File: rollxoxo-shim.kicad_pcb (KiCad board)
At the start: 4 copper layers, 29 x 42 mm, 68 parts, among them J1 USB_C_Receptacle_USB2.0_14P, J2 Conn_01x02, J3 Conn_01x10, J4 Conn_01x01, J5 Conn_01x10, J6 Conn_01x03, J7 Conn_01x01, SW1 SW_Push, SW2 SW_Push, U1 SN74LV1T125DBV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

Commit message: pcb: reorganize programmable gpios
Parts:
- moved R9 19.0 mm to (80.7, 153.8)
- moved R8 17.0 mm to (80.8, 154.8), turned to 0 degrees
- moved C19 0.25 mm to (80.8, 152.0)
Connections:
- U6 pad 14: /FLASH -> unconnected-(U6-GPIO9/ADC1_CH8-Pad14)
- U6 pad 6: unconnected-(U6-GPIO1/ADC1_CH0-Pad6) -> /FLASH
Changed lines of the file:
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@@
 	(footprint "Capacitor_SMD:C_0402_1005Metric"
 		(layer "F.Cu")
-		(at 80.75 152.25)
+		(at 80.75 152)
 		(descr "Capacitor SMD 0402 (1005 Metric), square (rectangular) end terminal, IPC-7351 nominal, (Body size source: IPC-SM-782 page 76, https://www.pcb-3d.com/wordpress/wp-content/uploads/ipc-sm-782a_amendment_1_and_2.pdf)")
 		(tags "capacitor")
@@
 			(layers "F.Cu" "F.Mask" "F.Paste")
 			(roundrect_rratio 0.25)
-			(net "unconnected-(U6-GPIO1{slash}ADC1_CH0-Pad6)")
+			(net "/FLASH")
 			(pinfunction "GPIO1/ADC1_CH0_6")
-			(pintype "bidirectional+no_connect")
+			(pintype "bidirectional")
 		)
 		(pad "7" smd roundrect
@@
 			(layers "F.Cu" "F.Mask" "F.Paste")
 			(roundrect_rratio 0.25)
-			(net "/FLASH")
+			(net "unconnected-(U6-GPIO9{slash}ADC1_CH8-Pad14)")
 			(pinfunction "GPIO9/ADC1_CH8_14")
-			(pintype "bidirectional")
+			(pintype "bidirectional+no_connect")
 		)
 		(pad "15" smd roundrect
@@
 	(footprint "Resistor_SMD:R_0402_1005Metric"
 		(layer "F.Cu")
-		(at 61.75 154.5)
+		(at 80.74 153.75)
 		(descr "Resistor SMD 0402 (1005 Metric), square (rectangular) end terminal, IPC-7351 nominal, (Body size source: IPC-SM-782 page 72, https://www.pcb-3d.com/wordpress/wp-content/uploads/ipc-sm-782a_amendment_1_and_2.pdf)")
 		(tags "resistor")
@@
 	(footprint "Resistor_SMD:R_0402_1005Metric"
 		(layer "F.Cu")
-		(at 63.76 154.5 180)
+		(at 80.76 154.75)
 		(descr "Resistor SMD 0402 (1005 Metric), square (rectangular) end terminal, IPC-7351 nominal, (Body size source: IPC-SM-782 page 72, https://www.pcb-3d.com/wordpress/wp-content/uploads/ipc-sm-782a_amendment_1_and_2.pdf)")
 		(tags "resistor")
@@
 		)
 		(property "Basic" "Y"
-			(at 0 0 180)
+			(at 0 0 0)
 			(unlocked yes)
 			(layer "F.Fab")
@@
 		)
 		(property "JLCPCB Part #" "C25744"
-			(at 0 0 180)
+			(at 0 0 0)
 			(unlocked yes)
 			(layer "F.Fab")
@@
 		)
 		(property "Manufacturer" "Uniroyal Elec"
-			(at 0 0 180)
+			(at 0 0 0)
 			(unlocked yes)
 			(layer "F.Fab")
@@
 		)
 		(property "Manufacturer Part Number" "0402WGF1002TCE"
-			(at 0 0 180)
+			(at 0 0 0)
 			(unlocked yes)
 			(layer "F.Fab")
@@
 		(duplicate_pad_numbers_are_jumpers no)
 		(fp_line
-			(start -0.153641 0.38)
-			(end 0.153641 0.38)
+			(start -0.153641 -0.38)
+			(end 0.153641 -0.38)
 			(stroke
 				(width 0.12)
@@
 		)
 		(fp_line
-			(start -0.153641 -0.38)
-			(end 0.153641 -0.38)
+			(start -0.153641 0.38)
+			(end 0.153641 0.38)
 			(stroke
 				(width 0.12)
@@
 		)
 		(pad "1" smd roundrect
-			(at -0.51 0 180)
+			(at -0.51 0)
 			(size 0.54 0.64)
 			(layers "F.Cu" "F.Mask" "F.Paste")
@@
 		)
 		(pad "2" smd roundrect
-			(at 0.51 0 180)
+			(at 0.51 0)
 			(size 0.54 0.64)
 			(layers "F.Cu" "F.Mask" "F.Paste")
@@
 	)
 	(via
-		(at 81.25 153)
+		(at 81.25 152.75)
 		(size 0.7)
 		(drill 0.3)

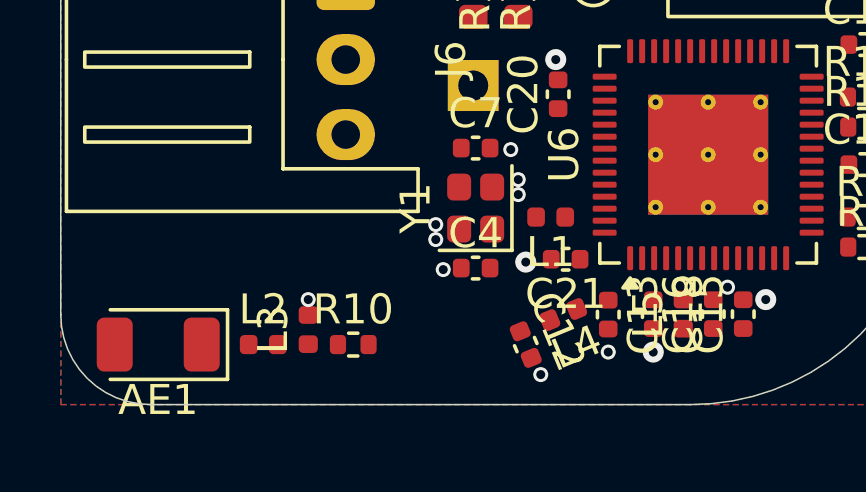
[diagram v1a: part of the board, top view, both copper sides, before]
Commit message: pcb: add rf routing
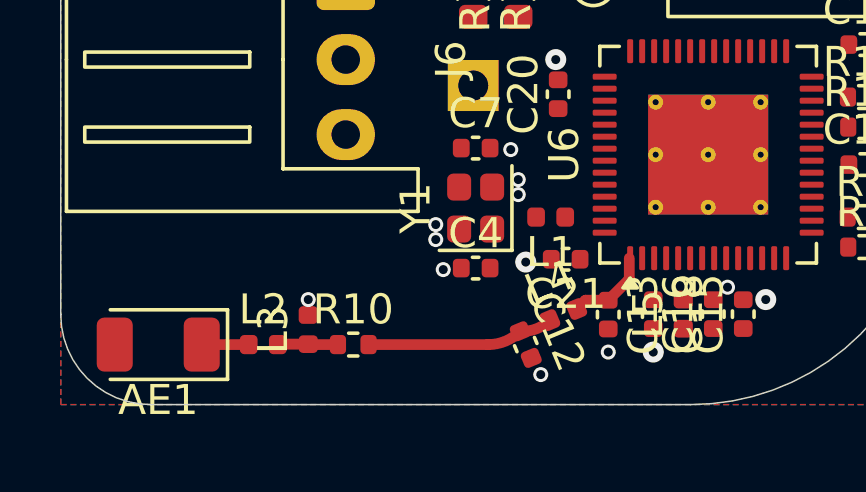
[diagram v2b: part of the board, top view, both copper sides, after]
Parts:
- turned L4 to 22.5 degrees
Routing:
- net /RF_TRANS: track 0.00 -> 6.25 mm
- net /RF_ESP: track 0.00 -> 2.86 mm
- net Net-(L2-Pad2): track 0.00 -> 2.02 mm
- net /RF_ANT: track 0.00 -> 1.56 mm
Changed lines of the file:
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@@
 	(footprint "Inductor_SMD:L_0402_1005Metric"
 		(layer "F.Cu")
-		(at 70.75 157 -157.5)
+		(at 70.75 157 22.5)
 		(descr "Inductor SMD 0402 (1005 Metric), square (rectangular) end terminal, IPC-7351 nominal, (Body size source: http://www.tortai-tech.com/upload/download/2011102023233369053.pdf)")
 		(tags "inductor")
@@
 		)
 		(property "Manufacturer" "Murata"
-			(at 0 0 202.5)
+			(at 0 0 22.5)
 			(unlocked yes)
 			(layer "F.Fab")
@@
 		)
 		(property "Manufacturer Part Number" "LQG15HS2N7S02D"
-			(at 0 0 202.5)
+			(at 0 0 22.5)
 			(unlocked yes)
 			(layer "F.Fab")
@@
 		)
 		(property "Basic" "X"
-			(at 0 0 202.5)
+			(at 0 0 22.5)
 			(unlocked yes)
 			(layer "F.Fab")
@@
 		)
 		(property "JLCPCB Part #" "C77108"
-			(at 0 0 202.5)
+			(at 0 0 22.5)
 			(unlocked yes)
 			(layer "F.Fab")
@@
 		)
 		(pad "1" smd roundrect
-			(at -0.485 0.000001 202.5)
+			(at -0.485 0.000001 22.5)
 			(size 0.59 0.64)
 			(layers "F.Cu" "F.Mask" "F.Paste")
@@
 		)
 		(pad "2" smd roundrect
-			(at 0.485 -0.000001 202.5)
+			(at 0.485 -0.000001 22.5)
 			(size 0.59 0.64)
 			(layers "F.Cu" "F.Mask" "F.Paste")
@@
 		(net "GND")
 	)
+	(segment
+		(start 60.265 158)
+		(end 58.7 158)
+		(width 0.359)
+		(layer "F.Cu")
+		(net "/RF_ANT")
+	)
+	(segment
+		(start 63.24 158)
+		(end 62.265 158)
+		(width 0.359)
+		(layer "F.Cu")
+		(net "Net-(L2-Pad2)")
+	)
+	(segment
+		(start 62.265 158)
+		(end 62.25 157.985)
+		(width 0.359)
+		(layer "F.Cu")
+		(net "Net-(L2-Pad2)")
+	)
+	(segment
+		(start 61.25 157.985)
+		(end 61.235 158)
+		(width 0.359)
+		(layer "F.Cu")
+		(net "Net-(L2-Pad2)")
+	)
+	(segment
+		(start 62.25 157.985)
+		(end 61.25 157.985)
+		(width 0.359)
+		(layer "F.Cu")
+		(net "Net-(L2-Pad2)")
+	)
+	(segment
+		(start 71.492479 156.52)
+		(end 71.198081 156.814398)
+		(width 0.359)
+		(layer "F.Cu")
+		(net "/RF_ESP")
+	)
+	(segment
+		(start 72.9505 155.8195)
+		(end 72.9505 155.12)
+		(width 0.359)
+		(layer "F.Cu")
+		(net "/RF_ESP")
+	)
+	(segment
+		(start 72.25 156.52)
+		(end 72.9505 155.8195)
+		(width 0.359)
+		(layer "F.Cu")
+		(net "/RF_ESP")
+	)
+	(segment
+		(start 72.25 156.52)
+		(end 71.492479 156.52)
+		(width 0.359)
+		(layer "F.Cu")
+		(net "/RF_ESP")
+	)
+	(segment
+		(start 69.4064 157.556538)
+		(end 69.316312 157.556538)
+		(width 0.359)
+		(layer "F.Cu")
+		(net "/RF_TRANS")
+	)
+	(segment
+		(start 68.2457 158)
+		(end 64.26 158)
+		(width 0.359)
+		(layer "F.Cu")
+		(net "/RF_TRANS")
+	)
+	(arc
+		(start 70.301919 157.185602)
+		(mid 69.891051 157.460135)
+		(end 69.4064 157.556538)
+		(width 0.359)
+		(layer "F.Cu")
+		(net "/RF_TRANS")
+	)
+	(arc
+		(start 69.316312 157.556538)
+		(mid 68.825111 157.884748)
+		(end 68.2457 158)
+		(width 0.359)
+		(layer "F.Cu")
+		(net "/RF_TRANS")
+	)
 	(zone

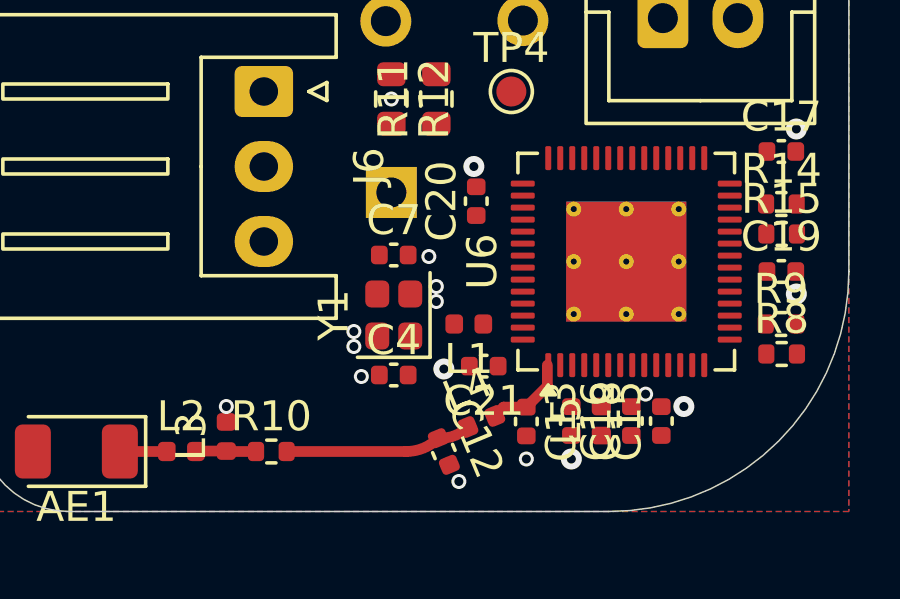
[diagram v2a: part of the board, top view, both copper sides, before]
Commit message: pcb: add rf routing
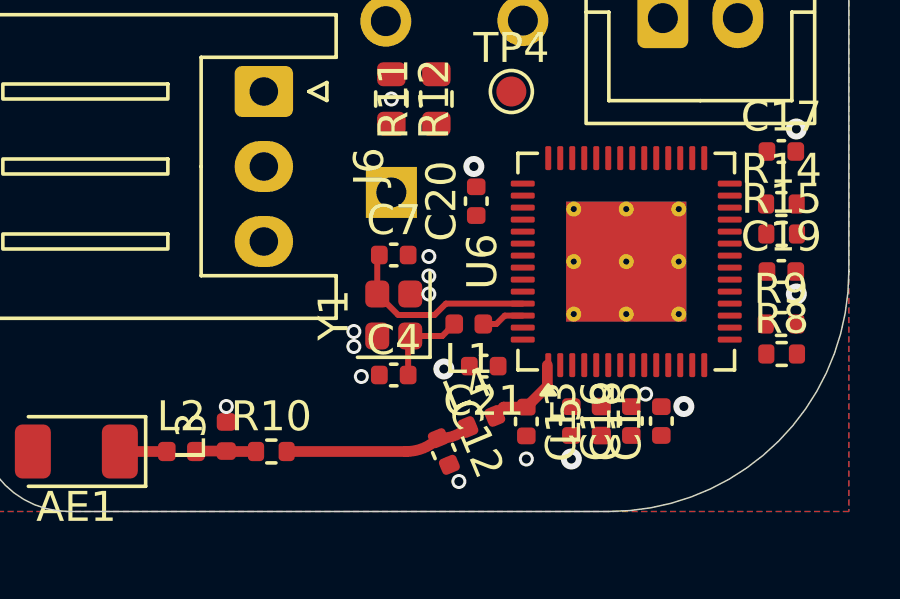
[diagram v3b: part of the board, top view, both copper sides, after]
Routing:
- net /XTAL_N: track 0.00 -> 6.63 mm
- net /XTAL_PL: track 0.00 -> 2.96 mm
- net /XTAL_P: track 0.00 -> 1.43 mm
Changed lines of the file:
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@@
-	)
-	(via
-		(at 69.25 153)
-		(size 0.5)
-		(drill 0.3)
-		(layers "F.Cu" "B.Cu")
-		(free yes)
-		(net "GND")
 	)
 	(via
@@
 	)
 	(via
+		(at 69 152.75)
+		(size 0.5)
+		(drill 0.3)
+		(layers "F.Cu" "B.Cu")
+		(free yes)
+		(net "GND")
+	)
+	(via
 		(at 75 141.25)
 		(size 0.9)
@@
 	)
 	(via
-		(at 69.25 152.5)
+		(at 69 152.150003)
 		(size 0.5)
 		(drill 0.3)
@@
 		(free yes)
 		(net "GND")
+	)
+	(segment
+		(start 67.28 151.52)
+		(end 67.35 151.45)
+		(width 0.2)
+		(layer "F.Cu")
+		(net "/XTAL_N")
+	)
+	(segment
+		(start 69.19 153.45)
+		(end 67.98 153.45)
+		(width 0.2)
+		(layer "F.Cu")
+		(net "/XTAL_N")
+	)
+	(segment
+		(start 69.57 153.07)
+		(end 69.19 153.45)
+		(width 0.2)
+		(layer "F.Cu")
+		(net "/XTAL_N")
+	)
+	(segment
+		(start 72.13 153.07)
+		(end 69.57 153.07)
+		(width 0.2)
+		(layer "F.Cu")
+		(net "/XTAL_N")
+	)
+	(segment
+		(start 67.98 153.45)
+		(end 67.28 152.75)
+		(width 0.2)
+		(layer "F.Cu")
+		(net "/XTAL_N")
+	)
+	(segment
+		(start 67.28 152.75)
+		(end 67.28 151.52)
+		(width 0.2)
+		(layer "F.Cu")
+		(net "/XTAL_N")
 	)
 	(segment
@@
 	)
 	(segment
+		(start 71.25 153.75)
+		(end 71.53 153.47)
+		(width 0.2)
+		(layer "F.Cu")
+		(net "/XTAL_P")
+	)
+	(segment
+		(start 70.815 153.75)
+		(end 71.25 153.75)
+		(width 0.2)
+		(layer "F.Cu")
+		(net "/XTAL_P")
+	)
+	(segment
+		(start 71.53 153.47)
+		(end 72.13 153.47)
+		(width 0.2)
+		(layer "F.Cu")
+		(net "/XTAL_P")
+	)
+	(segment
+		(start 69.845 153.75)
+		(end 69.445 154.15)
+		(width 0.2)
+		(layer "F.Cu")
+		(net "/XTAL_PL")
+	)
+	(segment
+		(start 69.445 154.15)
+		(end 68.38 154.15)
+		(width 0.2)
+		(layer "F.Cu")
+		(net "/XTAL_PL")
+	)
+	(segment
+		(start 68.31 154.22)
+		(end 68.38 154.15)
+		(width 0.2)
+		(layer "F.Cu")
+		(net "/XTAL_PL")
+	)
+	(segment
+		(start 68.31 155.45)
+		(end 68.31 154.22)
+		(width 0.2)
+		(layer "F.Cu")
+		(net "/XTAL_PL")
+	)
+	(segment

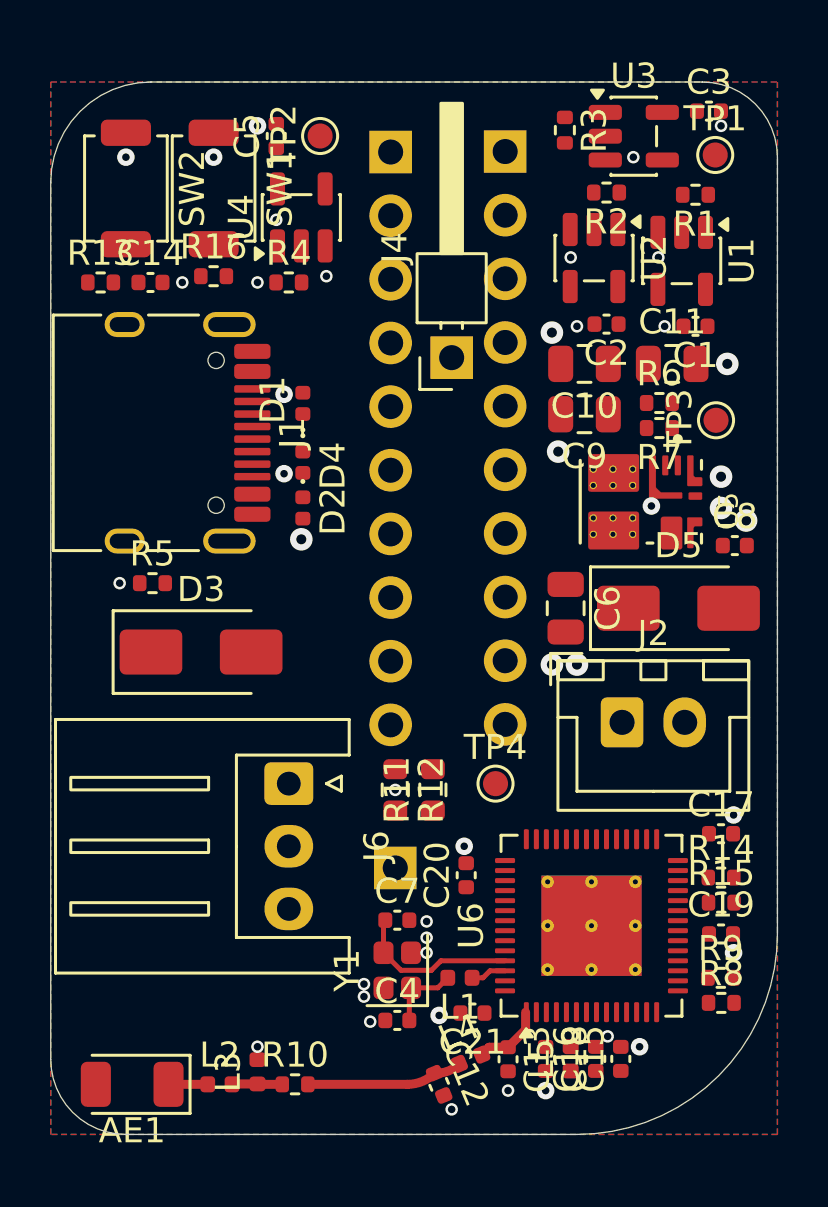
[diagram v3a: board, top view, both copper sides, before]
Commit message: pcb: add usb routing
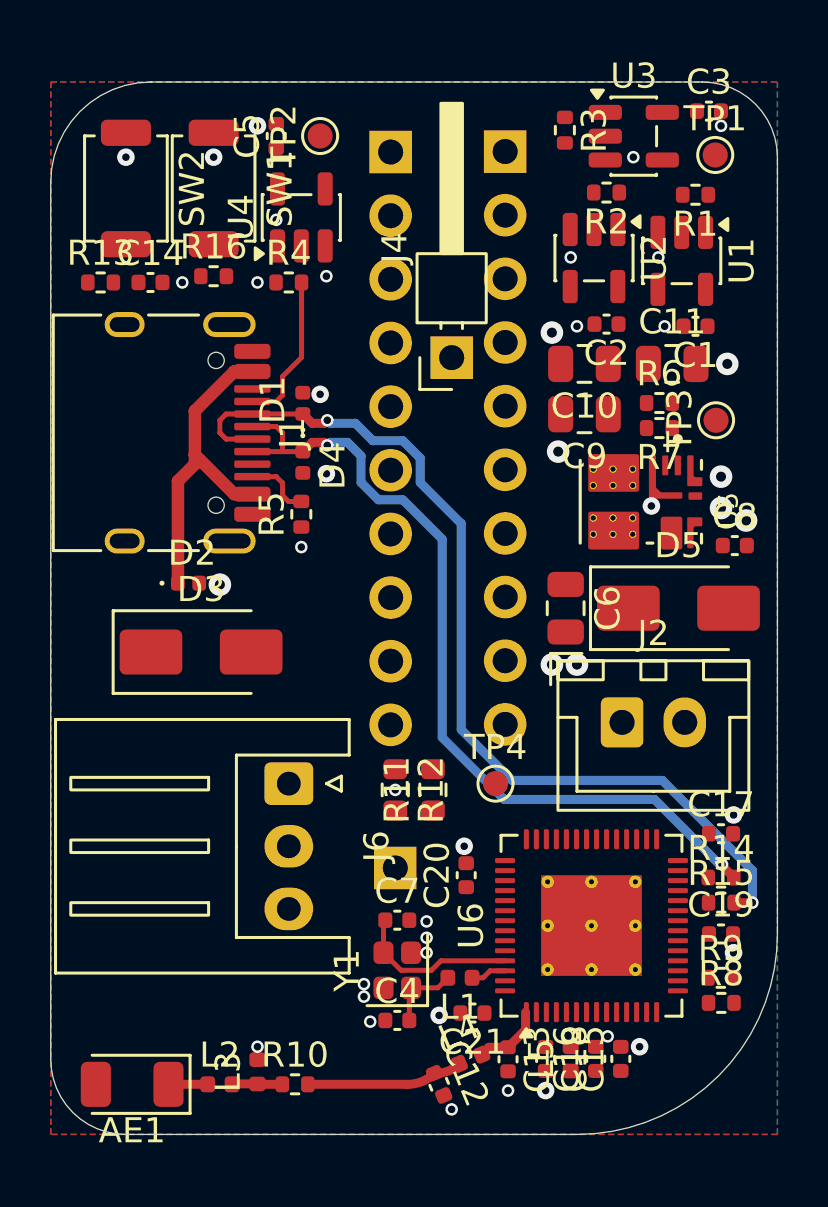
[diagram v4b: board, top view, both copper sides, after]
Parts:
- moved R5 6.55 mm to (64.0, 135.2), turned to 90 degrees
- moved D2 5.46 mm to (59.5, 138.0), turned to 0 degrees
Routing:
- net /D-: track 0.00 -> 38.3 mm, vias 0 -> 2
- net /D+: track 0.00 -> 34.0 mm, vias 0 -> 2
- net +Vbus: track 0.00 -> 13.0 mm
- net Net-(J1-CC1): track 0.00 -> 6.12 mm
- net Net-(J1-CC2): track 0.00 -> 2.66 mm

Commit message: pcb: add misc routing
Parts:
- moved TP4 0.56 mm to (71.2, 146.2)
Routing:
- net Net-(J4-Pin_1): track 0.00 -> 10.3 mm
- net /UP_BTN: track 0.00 -> 9.37 mm
- net /STOP_BTN: track 0.00 -> 8.91 mm
- net +3V3: track 0.00 -> 7.66 mm, vias 0 -> 1
- net +5V: track 0.00 -> 4.42 mm
- net /FLASH: track 0.00 -> 3.84 mm
- net /CHIP_PU: track 0.00 -> 3.46 mm
- net Net-(J7-Pin_1): track 0.00 -> 2.91 mm
- net Net-(U5-FB): track 0.00 -> 2.80 mm
- net /LIGHT: track 0.00 -> 2.20 mm
- net /UP: track 0.00 -> 1.70 mm
- net /REED_A: track 0.00 -> 1.57 mm
- net /DOWN: track 0.00 -> 1.55 mm
- net /STOP: track 0.00 -> 1.50 mm
- net /BOOT: track 0.00 -> 1.49 mm
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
